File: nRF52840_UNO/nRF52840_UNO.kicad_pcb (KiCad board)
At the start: 2 copper layers, 68.7 x 53.3 mm, 5 parts, among them J5 Conn_01x12, J6 Conn_01x16

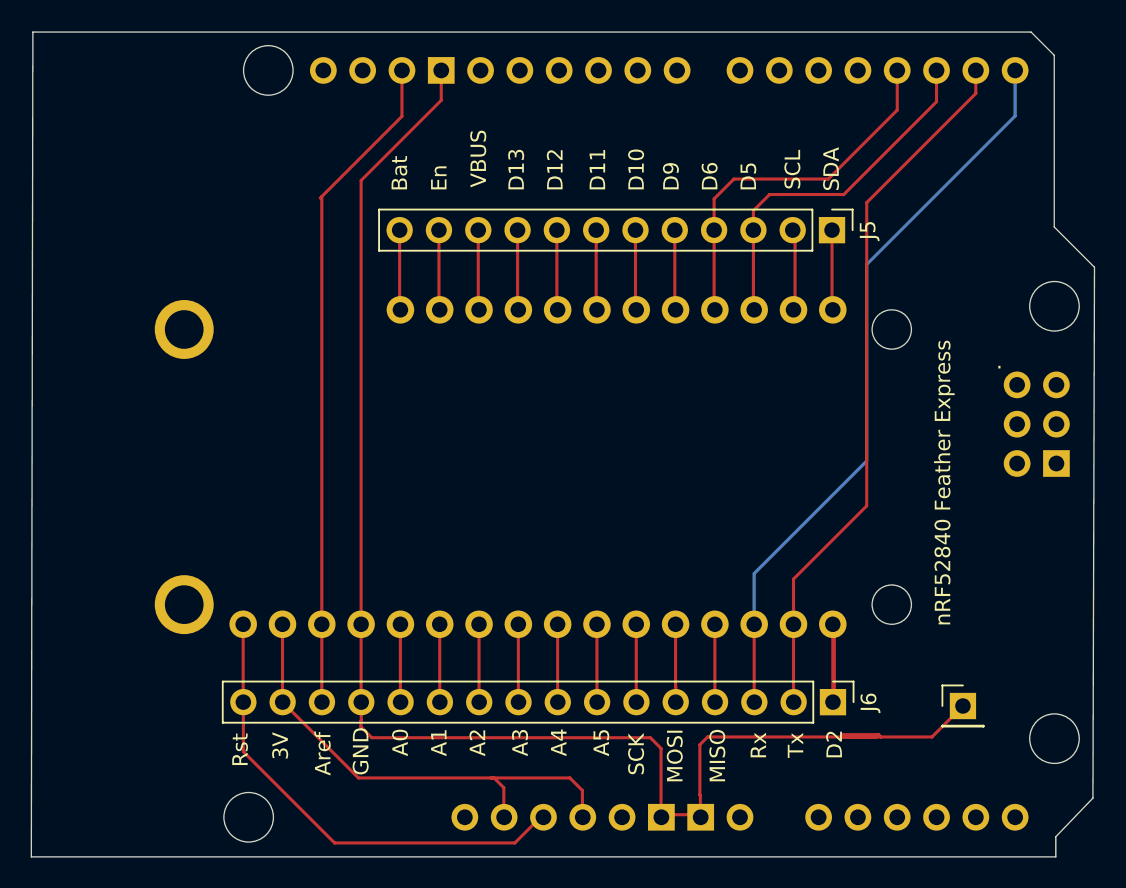
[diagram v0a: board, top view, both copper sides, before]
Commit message: Add 4bits adder
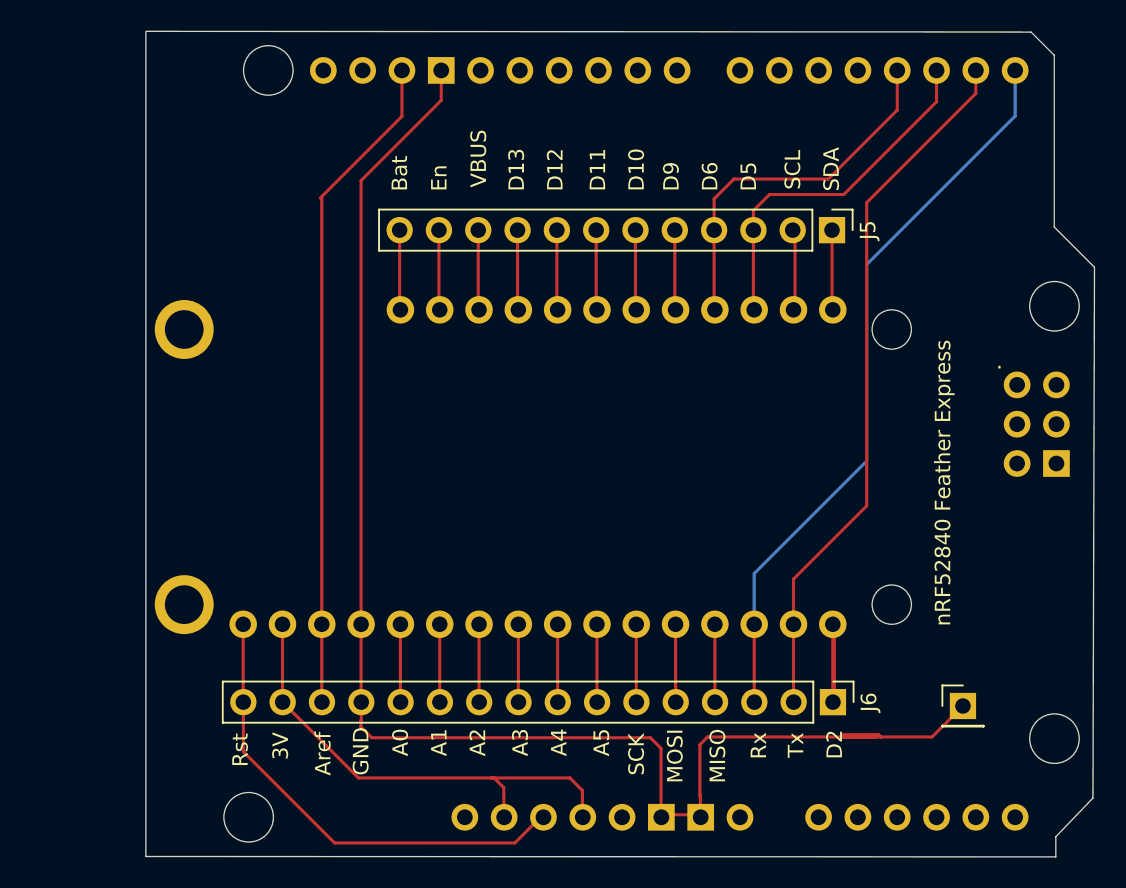
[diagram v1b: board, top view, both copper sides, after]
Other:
- board size 68.7 x 53.3 mm -> 61.3 x 53.3 mm
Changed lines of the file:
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@@
 	)
 	(gr_line
-		(start 57.8 82.5)
-		(end 57.9 29.2)
+		(start 65.202 82.474)
+		(end 65.202 29.154)
 		(stroke
 			(width 0.05)
@@
 	)
 	(gr_line
-		(start 57.9 29.2)
+		(start 65.252 29.154)
 		(end 122.4 29.2)
 		(stroke
@@
 	(gr_line
 		(start 124 82.5)
-		(end 57.8 82.5)
+		(end 65.202 82.474)
 		(stroke
 			(width 0.05)
